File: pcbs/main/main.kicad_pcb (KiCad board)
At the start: 2 copper layers, 114 x 123.3 mm, 60 parts, among them J1 JST_XH_B3B, J2 Jumpers, J3 JST_XH_B3B, J4 XT30PW-M, Q1 2SC945, Q2 2SC945, Q3 2SC945, Q4 2SC945, Q5 2SC945, Q6 2SC945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

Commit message: alteração antena
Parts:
- moved PCB2 2.85 mm to (76.1, 106.5)

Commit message: correção nrf24lo1
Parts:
- removed PCB1: ~, Oxebots:NRF24L01_PWR_ADP
- added REF**: NRF24L01_PWR_ADP, clipboard:147511f8-dbec-4e89-89ad-03905cd2e2e8, B.Cu at (76.2, 76.9)
- M1, M2, M3, M4: footprint Oxebots:HY-5_P2.00mm_Vertical -> Oxebots:NRF24L01
- moved PCB2 6.45 mm to (74.4, 100.2)

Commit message: Fix pcb
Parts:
- removed REF**: NRF24L01_PWR_ADP, clipboard:147511f8-dbec-4e89-89ad-03905cd2e2e8
- added PCB1: ~, Oxebots:NRF24L01_PWR_ADP, B.Cu at (76.6, 77.0)
- C10, C12, C13, C2, C4, C5, C6, C7, C8: footprint PCM_Capacitor_THT_AKL:C_Disc_D5.0mm_W2.5mm_P2.50mm -> Capacitor_THT:C_Disc_D5.0mm_W2.5mm_P2.50mm
- M1, M2, M3, M4: footprint Oxebots:NRF24L01 -> Oxebots:HY-5_P2.00mm_Vertical
- Q1, Q2, Q3, Q4, Q5, Q6, Q7, Q8: footprint PCM_Package_TO_SOT_THT_AKL:TO-92_Inline_Wide_ECB -> Package_TO_SOT_THT:TO-92L_Inline_Wide
- R1, R10, R11, R12, R13, R14, R15, R16, R2, R3, R4, R5, R6, R7, R8, R9: footprint PCM_Resistor_THT_AKL:R_Axial_DIN0207_L6.3mm_D2.5mm_P7.62mm_Horizontal -> Resistor_THT:R_Axial_DIN0207_L6.3mm_D2.5mm_P7.62mm_Horizontal
- moved C13 2.73 mm to (72.0, 68.6), turned to -90 degrees
- moved PCB2 0.52 mm to (74.9, 100.4)
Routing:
- net /esp32/RADIO.MOSI: track 42.9 -> 42.2 mm
- net /esp32/RADIO.MISO: track 62.5 -> 61.9 mm
- net /esp32/RADIO.IRQ: track 79.3 -> 78.7 mm
- net /esp32/RADIO.CLK: track 57.3 -> 56.7 mm
- net /esp32/RADIO.CE: track 62.0 -> 61.4 mm
- net /esp32/RADIO.CS: track 55.8 -> 55.2 mm

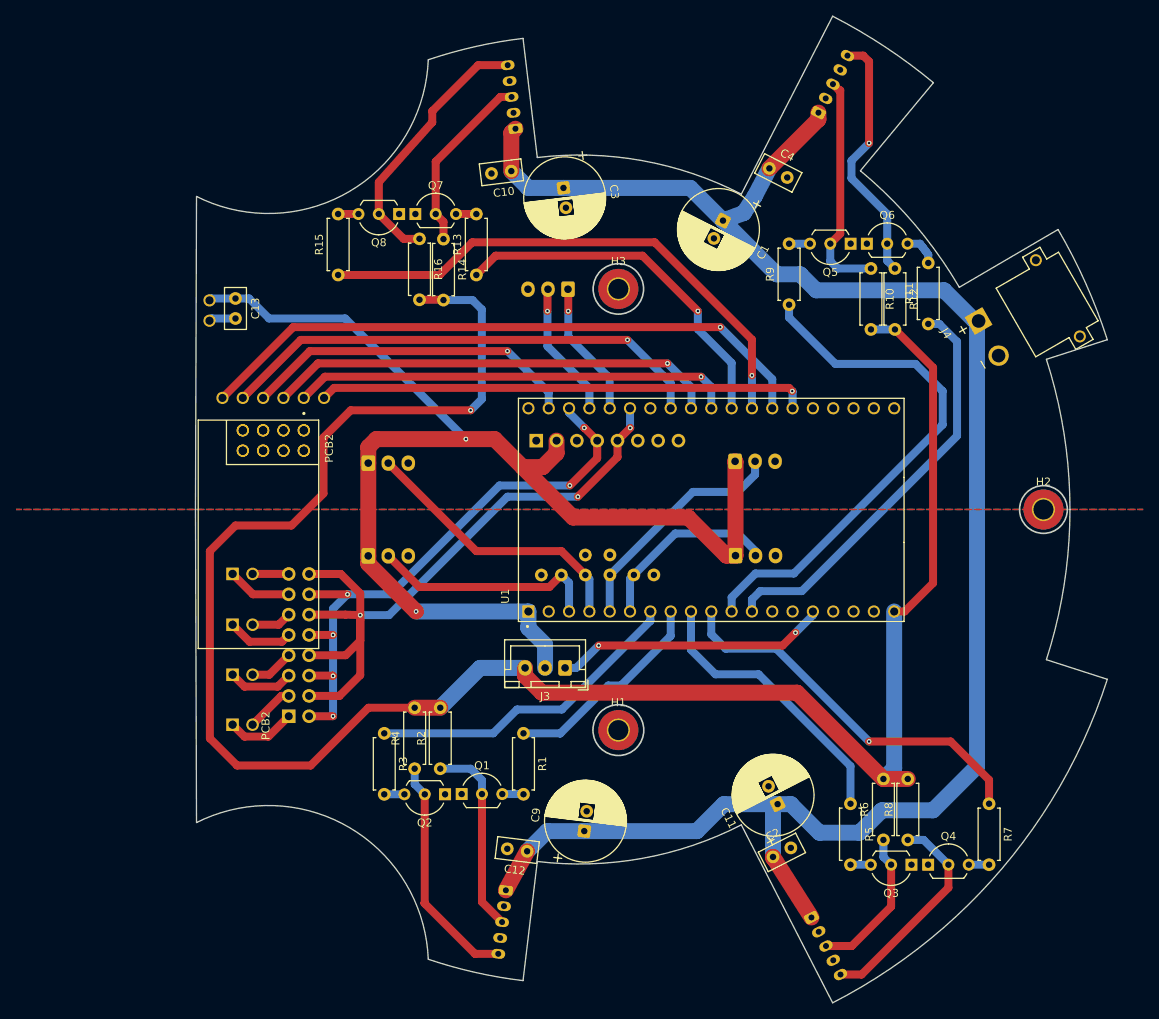
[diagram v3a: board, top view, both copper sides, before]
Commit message: adding ldo regulador to radio
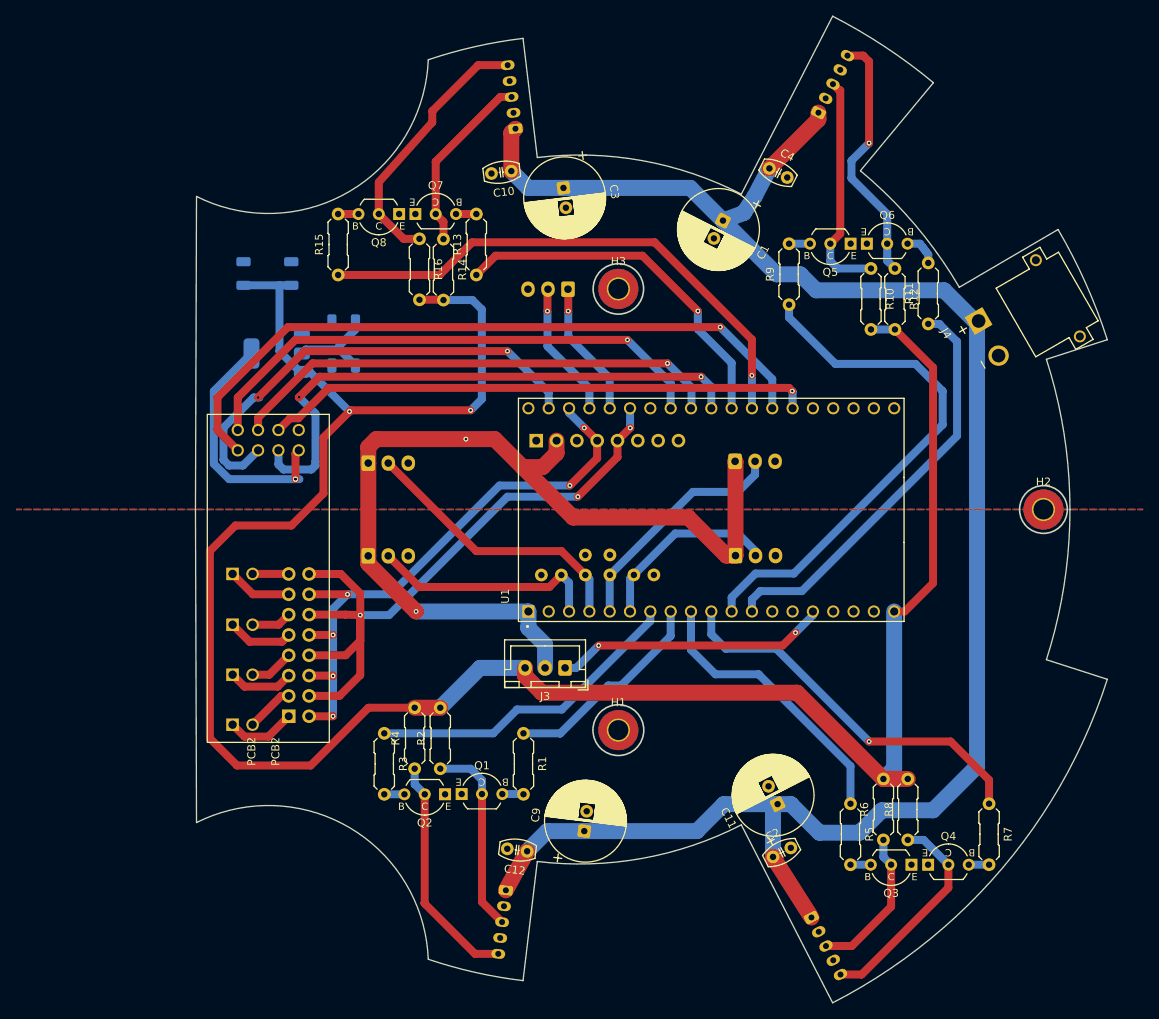
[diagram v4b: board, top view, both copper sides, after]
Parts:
- removed PCB1: ~, Oxebots:NRF24L01_PWR_ADP
- added C14: 10uF, Capacitor_SMD:C_1206_3216Metric, B.Cu at (79.0, 65.5)
- added C15: 10uF, Capacitor_SMD:C_1206_3216Metric, B.Cu at (85.5, 77.0)
- added C16: 10uF, Capacitor_SMD:C_1206_3216Metric, B.Cu at (85.5, 71.5)
- added U2: AMS1117-3.3, Package_TO_SOT_SMD:SOT-223-3_TabPin2, B.Cu at (77.2, 75.5)
- C10, C12, C2, C4, C5, C6, C7, C8: footprint Capacitor_THT:C_Disc_D5.0mm_W2.5mm_P2.50mm -> PCM_Capacitor_THT_AKL:C_Disc_D5.0mm_W2.5mm_P2.50mm
- C13: value 100 nF -> 10uF; footprint Capacitor_THT:C_Disc_D5.0mm_W2.5mm_P2.50mm -> Capacitor_SMD:C_1206_3216Metric; moved to B.Cu
- Q1, Q2, Q3, Q4, Q5, Q6, Q7, Q8: footprint Package_TO_SOT_THT:TO-92L_Inline_Wide -> PCM_Package_TO_SOT_THT_AKL:TO-92_Inline_Wide_ECB
- R1, R10, R11, R12, R13, R14, R15, R16, R2, R3, R4, R5, R6, R7, R8, R9: footprint Resistor_THT:R_Axial_DIN0207_L6.3mm_D2.5mm_P7.62mm_Horizontal -> PCM_Resistor_THT_AKL:R_Axial_DIN0207_L6.3mm_D2.5mm_P7.62mm_Horizontal
- moved PCB2 3.45 mm to (76.1, 103.6)
- moved C13 3.28 mm to (73.0, 65.5), turned to 90 degrees
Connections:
- C13 pad 1: +3.3V -> +5V
- PCB2 pad 1: Net-(PCB1-GND_{out}) -> GND
- PCB2 pad 2: Net-(PCB1-CE) -> /esp32/RADIO.CE
- PCB2 pad 3: Net-(PCB1-SCK) -> /esp32/RADIO.CLK
- PCB2 pad 4: Net-(PCB1-MISO) -> /esp32/RADIO.MISO
- PCB2 pad 5: Net-(PCB1-VCC_{out}) -> /radio/D3.3V
- PCB2 pad 6: Net-(PCB1-CSN) -> /esp32/RADIO.CS
- PCB2 pad 7: Net-(PCB1-MOSI) -> /esp32/RADIO.MOSI
- PCB2 pad 8: Net-(PCB1-IRQ) -> /esp32/RADIO.IRQ
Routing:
- net /radio/D3.3V: track 0.00 -> 43.1 mm, vias 0 -> 2
- net +3.3V: track 155.1 -> 115.7 mm
- net +5V: track 253.4 -> 279.5 mm, vias 1 -> 2
- net /esp32/RADIO.CS: track 55.2 -> 72.2 mm, vias 1 -> 2
- net /esp32/RADIO.MOSI: track 42.2 -> 58.3 mm, vias 1 -> 2
- net /esp32/RADIO.IRQ: track 78.7 -> 87.0 mm
- net /esp32/RADIO.CE: track 61.4 -> 68.7 mm
- net /esp32/RADIO.CLK: track 56.7 -> 62.4 mm
- net /esp32/RADIO.MISO: track 61.9 -> 66.5 mm
- net GND: track 3.57 -> 0.00 mm
